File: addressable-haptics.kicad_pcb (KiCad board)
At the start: 2 copper layers, 10.2 x 17.4 mm, 8 parts, among them J1 Conn_01x02, J2 Conn_01x03, J3 Conn_01x03, J4 SOICBite, Q1 Q_PMOS_GSD, U1 ATtiny10-TS

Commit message: Update PCB
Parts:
- Q1: value Q_PMOS_GSD -> Q_PNP_BEC
- moved J2 7.62 mm to (102.9, 46.0)
- moved J3 7.62 mm to (110.5, 46.0)
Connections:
- J4 pad 6: /signal_in -> /signal_out
- U1 pad 1: /signal_in -> /signal_out
- U1 pad 4: /signal_out -> /signal_in
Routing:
- net /signal_out: track 4.94 -> 11.3 mm, vias 0 -> 1
- net /signal_in: track 11.3 -> 4.94 mm, vias 1 -> 0

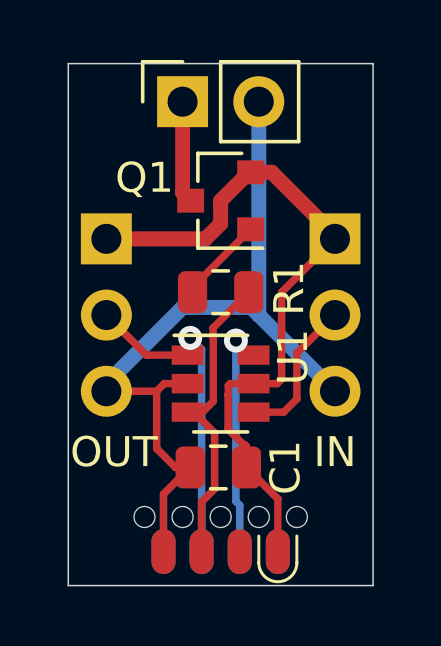
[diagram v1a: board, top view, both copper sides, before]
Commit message: Fixed schematic
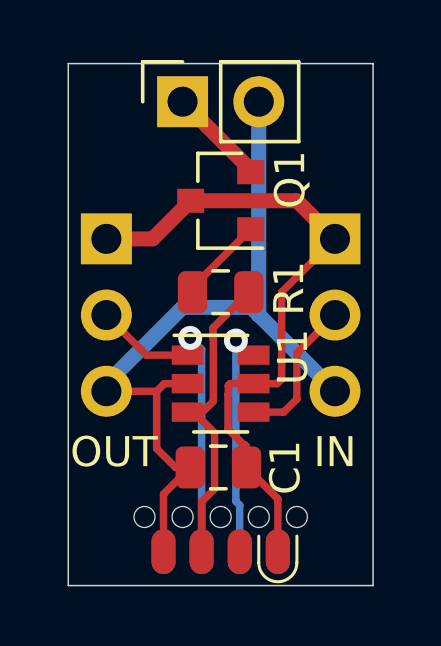
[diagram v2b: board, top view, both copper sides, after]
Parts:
- Q1: value Q_PNP_BEC -> Q_NMOS_GSD
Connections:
- Q1 pad 2: 3.3V -> /to_motor
- Q1 pad 3: /to_motor -> 3.3V
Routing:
- net 3.3V: track 23.1 -> 21.8 mm
